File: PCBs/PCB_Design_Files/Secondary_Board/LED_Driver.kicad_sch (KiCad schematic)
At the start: 14 parts, among them Q1 MMBT3904, Q2 MMBT3904, Q5 2N7002, Q6 BSS84, Q7 2N7002, Q8 BSS84, U8 OPA333AIDCKR

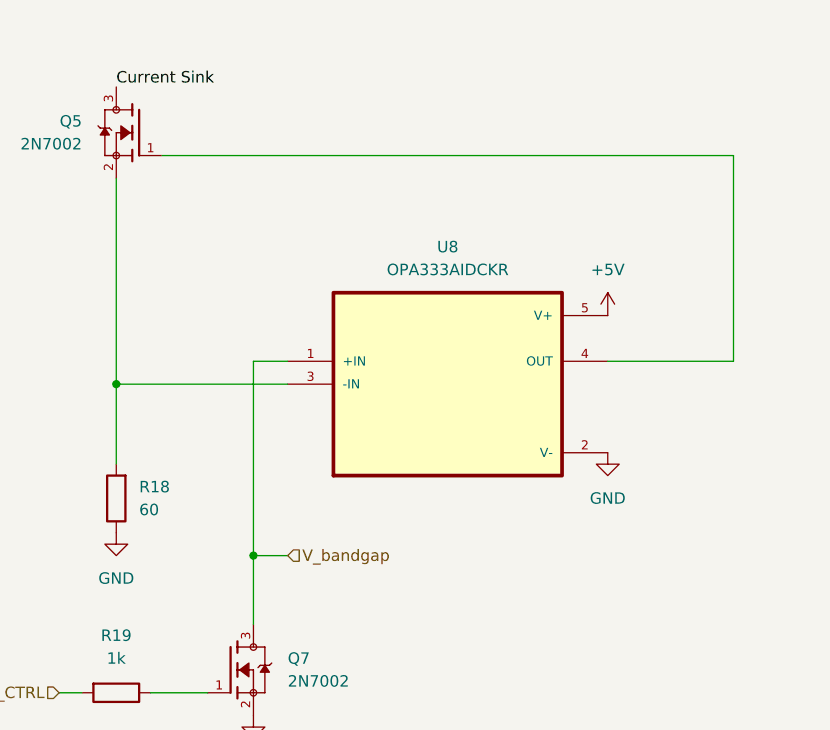
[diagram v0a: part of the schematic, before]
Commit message: add resistor and opa footprints
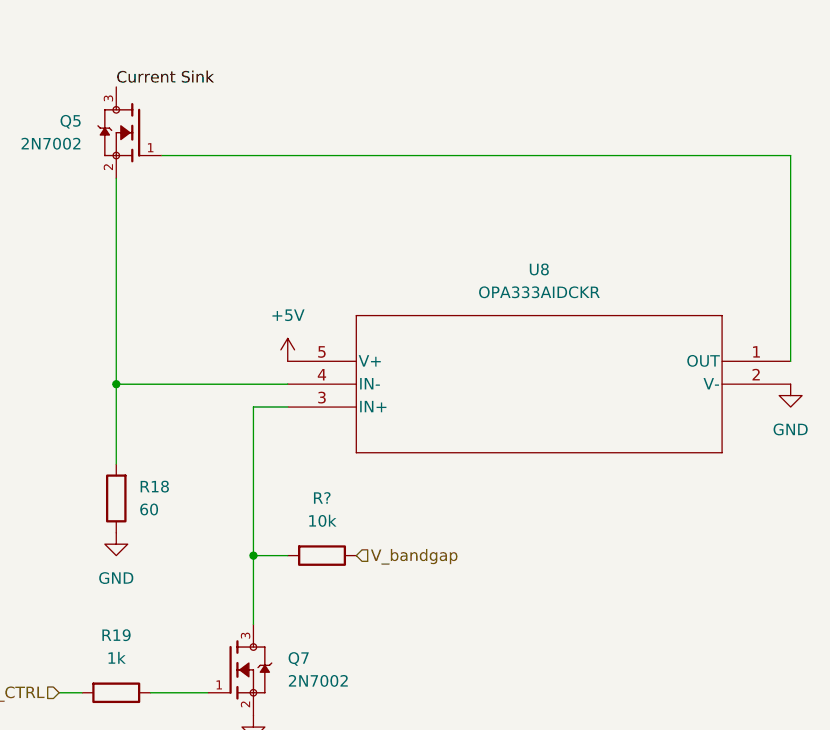
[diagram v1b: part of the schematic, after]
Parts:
- added R?: 10k, Resistor_SMD:R_0603_1608Metric_Pad0.98x0.95mm_HandSolder, symbol Device:R
- U8: footprint Project Footprints:OPA333 -> Project Footprints:DBV5; symbol Project_Symbols:OPA333AIDCKR -> Project_Symbols:OPA333AIDBVR
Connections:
- net V_bandgap: now also R?.1; no longer Q7.3, U8.1 (+IN)
- net at Q5.2, R18.2: now also U8.4 (IN-); no longer U8.3 (-IN)
- net at Q5.1: now also U8.1 (OUT); no longer U8.4 (OUT)
- new net: Q7.3, R?.2, U8.3 (IN+)
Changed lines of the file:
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@@
 	(paper "A4")
+	(junction
+		(at 176.53 102.87)
+		(diameter 0)
+		(color 0 0 0 0)
+	)
+	(junction
+		(at 99.06 115.57)
+		(diameter 0)
+		(color 0 0 0 0)
+	)
 	(junction
 		(at 191.77 121.92)
@@
 	)
 	(junction
-		(at 176.53 102.87)
-		(diameter 0)
-		(color 0 0 0 0)
-	)
-	(junction
-		(at 99.06 115.57)
-		(diameter 0)
-		(color 0 0 0 0)
-	)
-	(junction
 		(at 135.89 115.57)
 		(diameter 0)
@@
 	(wire
 		(pts
-			(xy 245.11 77.47) (xy 245.11 100.33)
-		)
-		(stroke
-			(width 0)
-			(type default)
-		)
-	)
-	(wire
-		(pts
 			(xy 191.77 121.92) (xy 191.77 129.54)
 		)
@@
 	(wire
 		(pts
-			(xy 181.61 77.47) (xy 245.11 77.47)
+			(xy 191.77 121.92) (xy 191.77 105.41)
+		)
+		(stroke
+			(width 0)
+			(type default)
+		)
+	)
+	(wire
+		(pts
+			(xy 181.61 77.47) (xy 251.46 77.47)
 		)
 		(stroke
@@
 	(wire
 		(pts
-			(xy 195.58 100.33) (xy 191.77 100.33)
-		)
-		(stroke
-			(width 0)
-			(type default)
-		)
-	)
-	(wire
-		(pts
 			(xy 87.63 127) (xy 91.44 127)
 		)
@@
 	(wire
 		(pts
-			(xy 245.11 100.33) (xy 231.14 100.33)
+			(xy 191.77 105.41) (xy 195.58 105.41)
 		)
 		(stroke
@@
 	(wire
 		(pts
-			(xy 191.77 100.33) (xy 191.77 121.92)
+			(xy 251.46 77.47) (xy 251.46 100.33)
 		)
 		(stroke
@@
 	(hierarchical_label "V_bandgap"
 		(shape input)
-		(at 195.58 121.92 0)
+		(at 203.2 121.92 0)
 		(effects
 			(font
@@
 				)
 			)
+			(project "LED_Driver"
+				(path "/ed36e940-b5c2-4fa7-8175-f729e6b712de"
+					(reference "R?")
+					(unit 1)
+				)
+			)
 		)
 	)
@@
 	(symbol
 		(lib_id "power:+5V")
-		(at 231.14 95.25 0)
+		(at 195.58 100.33 0)
 		(unit 1)
 		(exclude_from_sim no)
@@
 		(fields_autoplaced yes)
 		(property "Reference" "#PWR0118"
-			(at 231.14 99.06 0)
+			(at 195.58 104.14 0)
 			(effects
 				(font
@@
 		)
 		(property "Value" "+5V"
-			(at 231.14 90.17 0)
+			(at 195.58 95.25 0)
 			(effects
 				(font
@@
 		)
 		(property "Footprint" ""
-			(at 231.14 95.25 0)
+			(at 195.58 100.33 0)
 			(effects
 				(font
@@
 		)
 		(property "Datasheet" ""
-			(at 231.14 95.25 0)
+			(at 195.58 100.33 0)
 			(effects
 				(font
@@
 		)
 		(property "Description" "Power symbol creates a global label with name \"+5V\""
-			(at 231.14 95.25 0)
+			(at 195.58 100.33 0)
 			(effects
 				(font
@@
 	)
 	(symbol
-		(lib_id "Project_Symbols:OPA333AIDCKR")
-		(at 213.36 102.87 0)
+		(lib_id "Project_Symbols:OPA333AIDBVR")
+		(at 251.46 100.33 0)
+		(mirror y)
 		(unit 1)
 		(exclude_from_sim no)
@@
 		(on_board yes)
 		(dnp no)
-		(fields_autoplaced yes)
 		(property "Reference" "U8"
-			(at 213.36 87.63 0)
+			(at 223.52 90.17 0)
 			(effects
 				(font
@@
 		)
 		(property "Value" "OPA333AIDCKR"
-			(at 213.36 90.17 0)
-			(effects
-				(font
-					(size 1.27 1.27)
-				)
-			)
-		)
-		(property "Footprint" "Project Footprints:OPA333"
-			(at 212.852 121.412 0)
-			(effects
-				(font
-					(size 1.27 1.27)
-				)
-				(justify bottom)
-				(hide yes)
-			)
-		)
-		(property "Datasheet" ""
-			(at 213.36 102.87 0)
-			(effects
-				(font
-					(size 1.27 1.27)
+			(at 223.52 92.71 0)
+			(effects
+				(font
+					(size 1.27 1.27)
+				)
+			)
+		)
+		(property "Footprint" "Project Footprints:DBV5"
+			(at 251.46 100.33 0)
+			(effects
+				(font
+					(size 1.27 1.27)
+					(italic yes)
+				)
+				(hide yes)
+			)
+		)
+		(property "Datasheet" "https://www.ti.com/lit/gpn/opa333"
+			(at 251.46 100.33 0)
+			(effects
+				(font
+					(size 1.27 1.27)
+					(italic yes)
 				)
 				(hide yes)
@@
 		)
 		(property "Description" ""
-			(at 213.36 102.87 0)
+			(at 251.46 100.33 0)
 			(effects
 				(font
@@
 	)
 	(symbol
+		(lib_id "Device:R")
+		(at 199.39 121.92 270)
+		(unit 1)
+		(exclude_from_sim no)
+		(in_bom yes)
+		(on_board yes)
+		(dnp no)
+		(fields_autoplaced yes)
+		(property "Reference" "R?"
+			(at 199.39 115.57 90)
+			(effects
+				(font
+					(size 1.27 1.27)
+				)
+			)
+		)
+		(property "Value" "10k"
+			(at 199.39 118.11 90)
+			(effects
+				(font
+					(size 1.27 1.27)
+				)
+			)
+		)
+		(property "Footprint" "Resistor_SMD:R_0603_1608Metric_Pad0.98x0.95mm_HandSolder"
+			(at 199.39 120.142 90)
+			(effects
+				(font
+					(size 1.27 1.27)
+				)
+				(hide yes)
+			)
+		)
+		(property "Datasheet" "~"
+			(at 199.39 121.92 0)
+			(effects
+				(font
+					(size 1.27 1.27)
+				)
+				(hide yes)
+			)
+		)
+		(property "Description" "Resistor"
+			(at 199.39 121.92 0)
+			(effects
+				(font
+					(size 1.27 1.27)
+				)
+				(hide yes)
+			)
+		)
+		(pin "2"
+		)
+		(pin "1"
+		)
+		(instances
+			(project "Secondary_Board"
+				(path "/2f5986e4-77b2-4f5d-ab91-80ba6228eb8b/16ecf950-1853-427b-9137-65792483b2a5"
+					(reference "R?")
+					(unit 1)
+				)
+			)
+			(project "LED_Driver"
+				(path "/ed36e940-b5c2-4fa7-8175-f729e6b712de"
+					(reference "R6")
+					(unit 1)
+				)
+			)
+		)
+	)
+	(symbol
 		(lib_id "power:GND")
-		(at 231.14 110.49 0)
+		(at 251.46 102.87 0)
 		(unit 1)
 		(exclude_from_sim no)
@@
 		(fields_autoplaced yes)
 		(property "Reference" "#PWR0119"
-			(at 231.14 116.84 0)
+			(at 251.46 109.22 0)
 			(effects
 				(font
@@
 		)
 		(property "Value" "GND"
-			(at 231.14 115.57 0)
+			(at 251.46 107.95 0)
 			(effects
 				(font
@@
 		)
 		(property "Footprint" ""
-			(at 231.14 110.49 0)
+			(at 251.46 102.87 0)
 			(effects
 				(font
@@
 		)
 		(property "Datasheet" ""
-			(at 231.14 110.49 0)
+			(at 251.46 102.87 0)
 			(effects
 				(font
@@
 		)
 		(property "Description" "Power symbol creates a global label with name \"GND\" , ground"
-			(at 231.14 110.49 0)
-			(effects
-				(font
+			(at 251.46 102.87 0)
+			(effects
+				(font
